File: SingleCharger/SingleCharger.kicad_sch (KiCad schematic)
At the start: 9 parts, among them J2 Conn_01x03_Pin, J4 Conn_01x02_Pin, U2 PICO

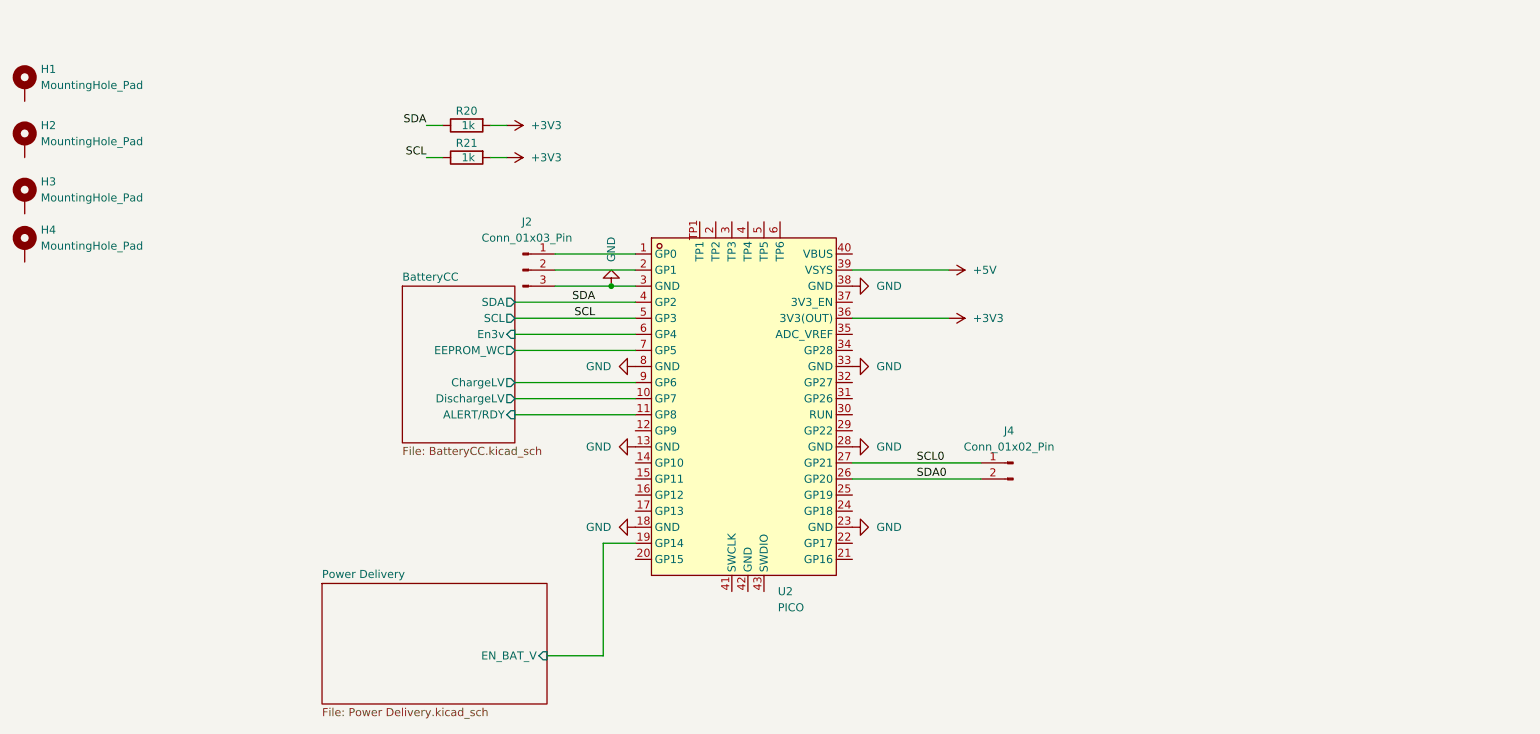
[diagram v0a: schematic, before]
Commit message: Started adding LEDS
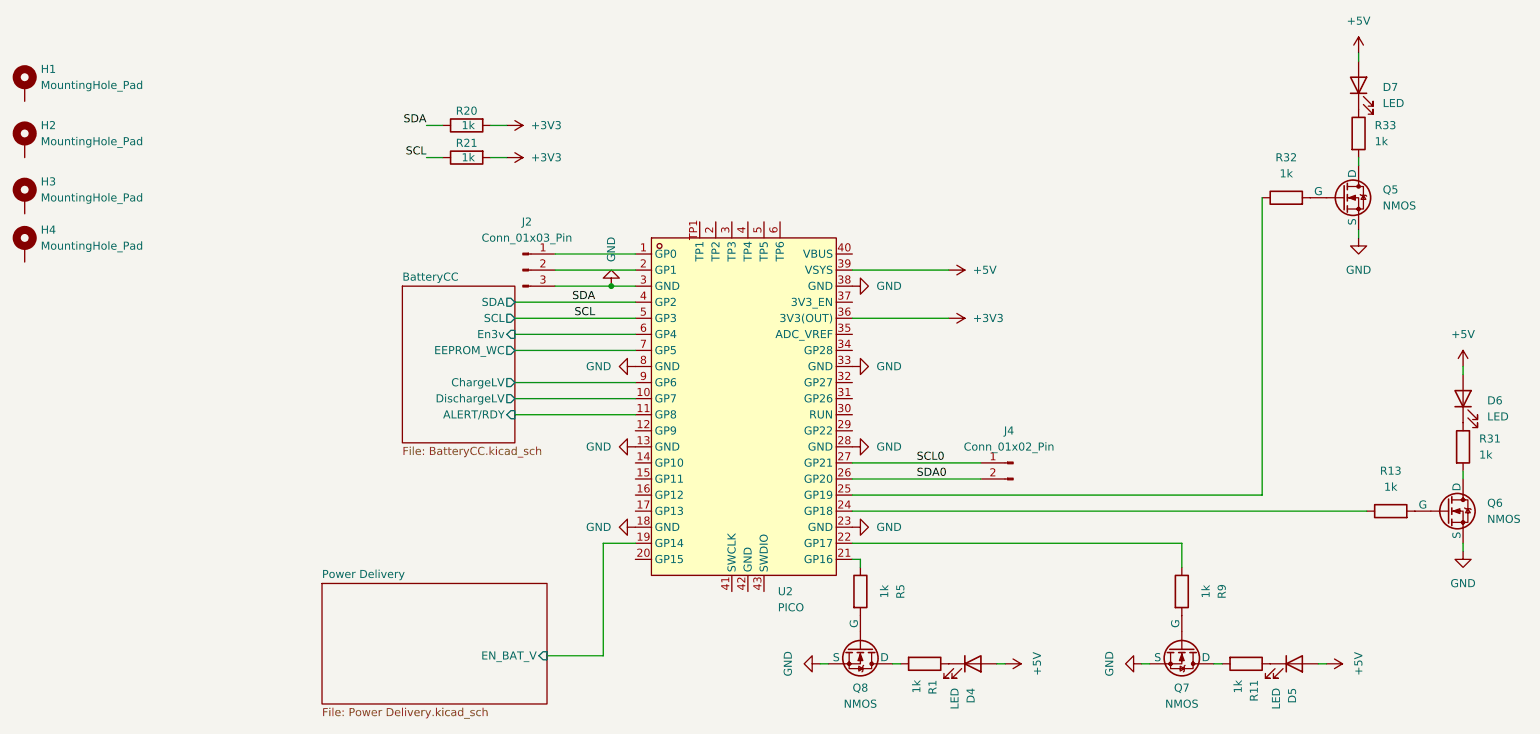
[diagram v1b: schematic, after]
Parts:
- added D4, D5, D6, D7: LED, LED_SMD:LED_1206_3216Metric, symbol Device:LED
- added Q5, Q6, Q7, Q8: NMOS, Package_TO_SOT_SMD:SOT-23, symbol Simulation_SPICE:NMOS
- added R1, R11, R13, R31, R32, R33, R5, R9: 1k, Resistor_SMD:R_1206_3216Metric, symbol Device:R
- R20, R21: footprint Resistor_SMD:R_1206_3216Metric_Pad1.30x1.75mm_HandSolder -> Resistor_SMD:R_1206_3216Metric
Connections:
- net +5V: now also D4.2 (A), D5.2 (A), D6.2 (A), D7.2 (A)
- net GND: now also Q5.2 (S), Q6.2 (S), Q7.2 (S), Q8.2 (S)
- net at U2.21 (GP16): now also R5.1
- net at U2.22 (GP17): now also R9.1
- net at U2.24 (GP18): now also R13.1
- net at U2.25 (GP19): now also R32.1
- new net: Q6.1 (G), R13.2
- new net: Q7.1 (G), R9.2
- new net: Q5.1 (G), R32.2
- new net: Q8.1 (G), R5.2
- new net: D4.1 (K), R1.1
- new net: Q8.3 (D), R1.2
- new net: Q5.3 (D), R33.2
- new net: D7.1 (K), R33.1
- new net: D5.1 (K), R11.1
- new net: Q7.3 (D), R11.2
- new net: Q6.3 (D), R31.2
- new net: D6.1 (K), R31.1

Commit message: Working on fixing PICO.
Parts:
- U2: footprint Module:RaspberryPi_Pico_Common_THT -> Module:RaspberryPi_Pico_SMD
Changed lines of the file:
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@@
 			)
 		)
-		(property "Footprint" "Module:RaspberryPi_Pico_Common_THT"
+		(property "Footprint" "Module:RaspberryPi_Pico_SMD"
 			(at 154.94 132.08 0)
 			(effects

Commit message: Finished with layout changes.
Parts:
- added J5: Conn_01x03_Pin, Connector_PinHeader_2.54mm:PinHeader_1x03_P2.54mm_Horizontal, symbol Connector:Conn_01x03_Pin
- J2: footprint Connector_PinHeader_2.54mm:PinHeader_1x03_P2.54mm_Vertical -> Connector_PinHeader_2.54mm:PinHeader_1x03_P2.54mm_Horizontal
- J4: footprint Connector_PinHeader_2.54mm:PinHeader_1x02_P2.54mm_Vertical -> Connector_PinHeader_2.54mm:PinHeader_1x02_P2.54mm_Horizontal
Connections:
- net at U2.41 (SWCLK): now also J5.1 (Pin_1)
- net at U2.42 (GND): now also J5.2 (Pin_2)
- net at U2.43 (SWDIO): now also J5.3 (Pin_3)
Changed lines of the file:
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@@
+	(wire
+		(pts
+			(xy 152.4 129.54) (xy 152.4 124.46)
+		)
+		(stroke
+			(width 0)
+			(type default)
+		)
+	)
 	(wire
 		(pts
@@
 	(wire
 		(pts
+			(xy 157.48 129.54) (xy 157.48 124.46)
+		)
+		(stroke
+			(width 0)
+			(type default)
+		)
+	)
+	(wire
+		(pts
 			(xy 171.45 109.22) (xy 236.22 109.22)
 		)
@@
 		(pts
 			(xy 116.84 55.88) (xy 114.3 55.88)
+		)
+		(stroke
+			(width 0)
+			(type default)
+		)
+	)
+	(wire
+		(pts
+			(xy 154.94 129.54) (xy 154.94 124.46)
 		)
 		(stroke
@@
 			)
 		)
-		(property "Footprint" "Connector_PinHeader_2.54mm:PinHeader_1x03_P2.54mm_Vertical"
+		(property "Footprint" "Connector_PinHeader_2.54mm:PinHeader_1x03_P2.54mm_Horizontal"
 			(at 119.38 73.66 0)
 			(effects
@@
 			)
 		)
-		(property "Footprint" "Connector_PinHeader_2.54mm:PinHeader_1x02_P2.54mm_Vertical"
+		(property "Footprint" "Connector_PinHeader_2.54mm:PinHeader_1x02_P2.54mm_Horizontal"
 			(at 196.85 104.14 0)
 			(effects
@@
 					(unit 1)
 				)
+			)
+		)
+	)
+	(symbol
+		(lib_id "Connector:Conn_01x03_Pin")
+		(at 154.94 134.62 90)
+		(unit 1)
+		(exclude_from_sim no)
+		(in_bom yes)
+		(on_board yes)
+		(dnp no)
+		(fields_autoplaced yes)
+		(property "Reference" "J5"
+			(at 154.94 137.16 90)
+			(effects
+				(font
+					(size 1.27 1.27)
+				)
+			)
+		)
+		(property "Value" "Conn_01x03_Pin"
+			(at 154.94 139.7 90)
+			(effects
+				(font
+					(size 1.27 1.27)
+				)
+			)
+		)
+		(property "Footprint" "Connector_PinHeader_2.54mm:PinHeader_1x03_P2.54mm_Horizontal"
+			(at 154.94 134.62 0)
+			(effects
+				(font
+					(size 1.27 1.27)
+				)
+				(hide yes)
+			)
+		)
+		(property "Datasheet" "~"
+			(at 154.94 134.62 0)
+			(effects
+				(font
+					(size 1.27 1.27)
+				)
+				(hide yes)
+			)
+		)
+		(property "Description" "Generic connector, single row, 01x03, script generated"
+			(at 154.94 134.62 0)
+			(effects
+				(font
+					(size 1.27 1.27)
+				)
+				(hide yes)
+			)
+		)
+		(pin "1"
+		)
+		(pin "2"
+		)
+		(pin "3"
+		)
+		(instances
+			(project "SingleCharger"
+				(path "/e710e346-5907-4662-9fec-fc15df74dc9e"
+					(reference "J5")
+					(unit 1)
+				)
